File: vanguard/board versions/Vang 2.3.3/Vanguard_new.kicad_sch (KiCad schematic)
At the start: 98 parts, among them J1 USB_C_Receptacle_USB2.0_16P, J2 Micro_SD_Card_Det1, J3 Conn_02x03_Odd_Even, J4 Conn_01x03, J5 Conn_01x03, J6 Conn_01x03, J7 Conn_01x02_Pin, Q1 BSS138, Q2 BSS138, Q3 BSS138, Q4 BSS138, SW1 SW_Push, U1 TXB0104D, U11 TPS82130SILR, U12 AP2112K-3.3, U3 ATSAMD11D14A-M, U4 BMP390L, U5 BD1020HFV-TR, U6 AT25DF641A-SH-T, U7 ATmega4809-A, U8 BNO055, U9 TPS61092, Y1 Crystal

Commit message: e
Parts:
- removed D11: LED, LED_SMD:LED_0201_0603Metric, symbol Device:LED
- removed R32: 330, Resistor_SMD:R_0402_1005Metric, symbol Device:R
- removed SW1: SW_Push, symbol Switch:SW_Push
- added C10: 1uF, symbol Device:C
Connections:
- net GND: now also C10.2
- net at C16.1, R35.1, R38.1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: now also C10.1
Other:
- moved on the sheet: C18, D13, R38, U12

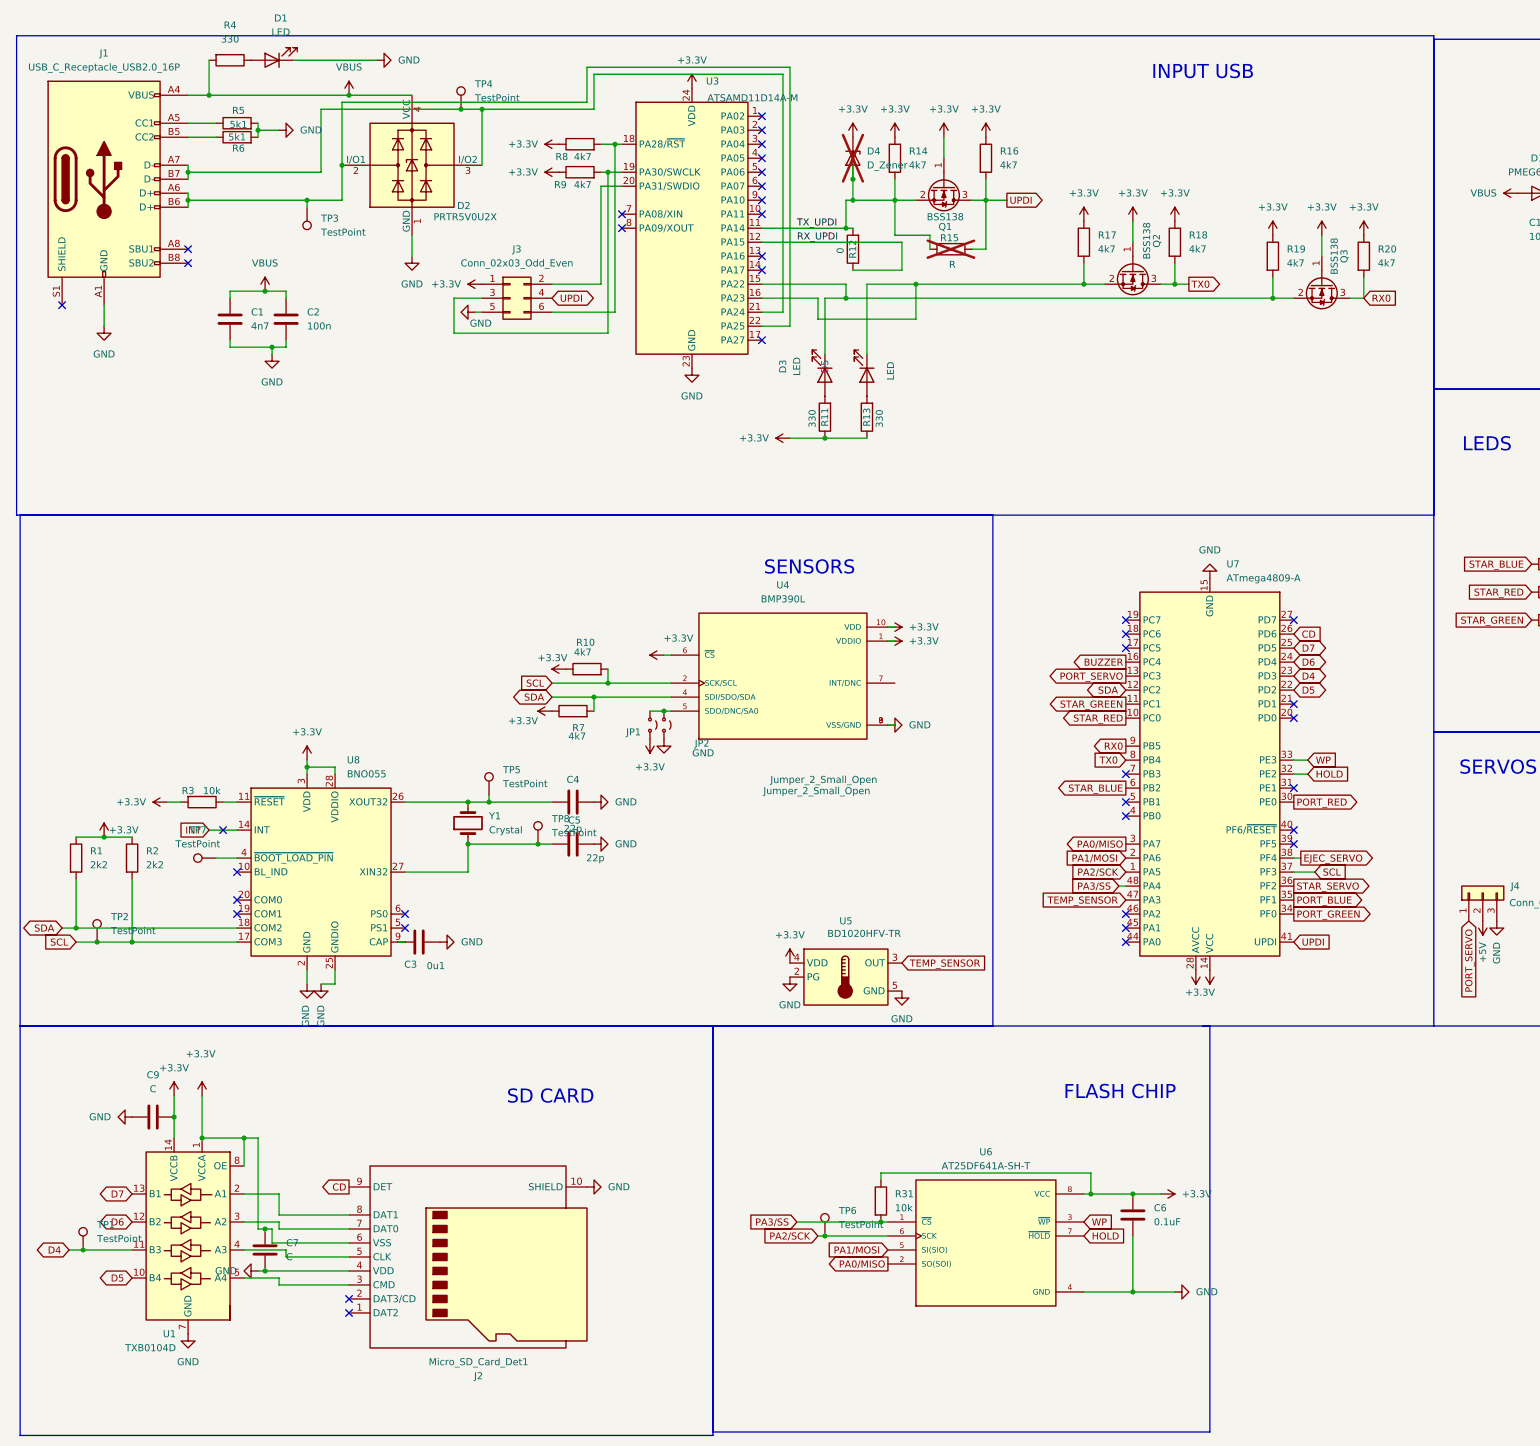
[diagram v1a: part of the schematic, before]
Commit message: updated sch caps
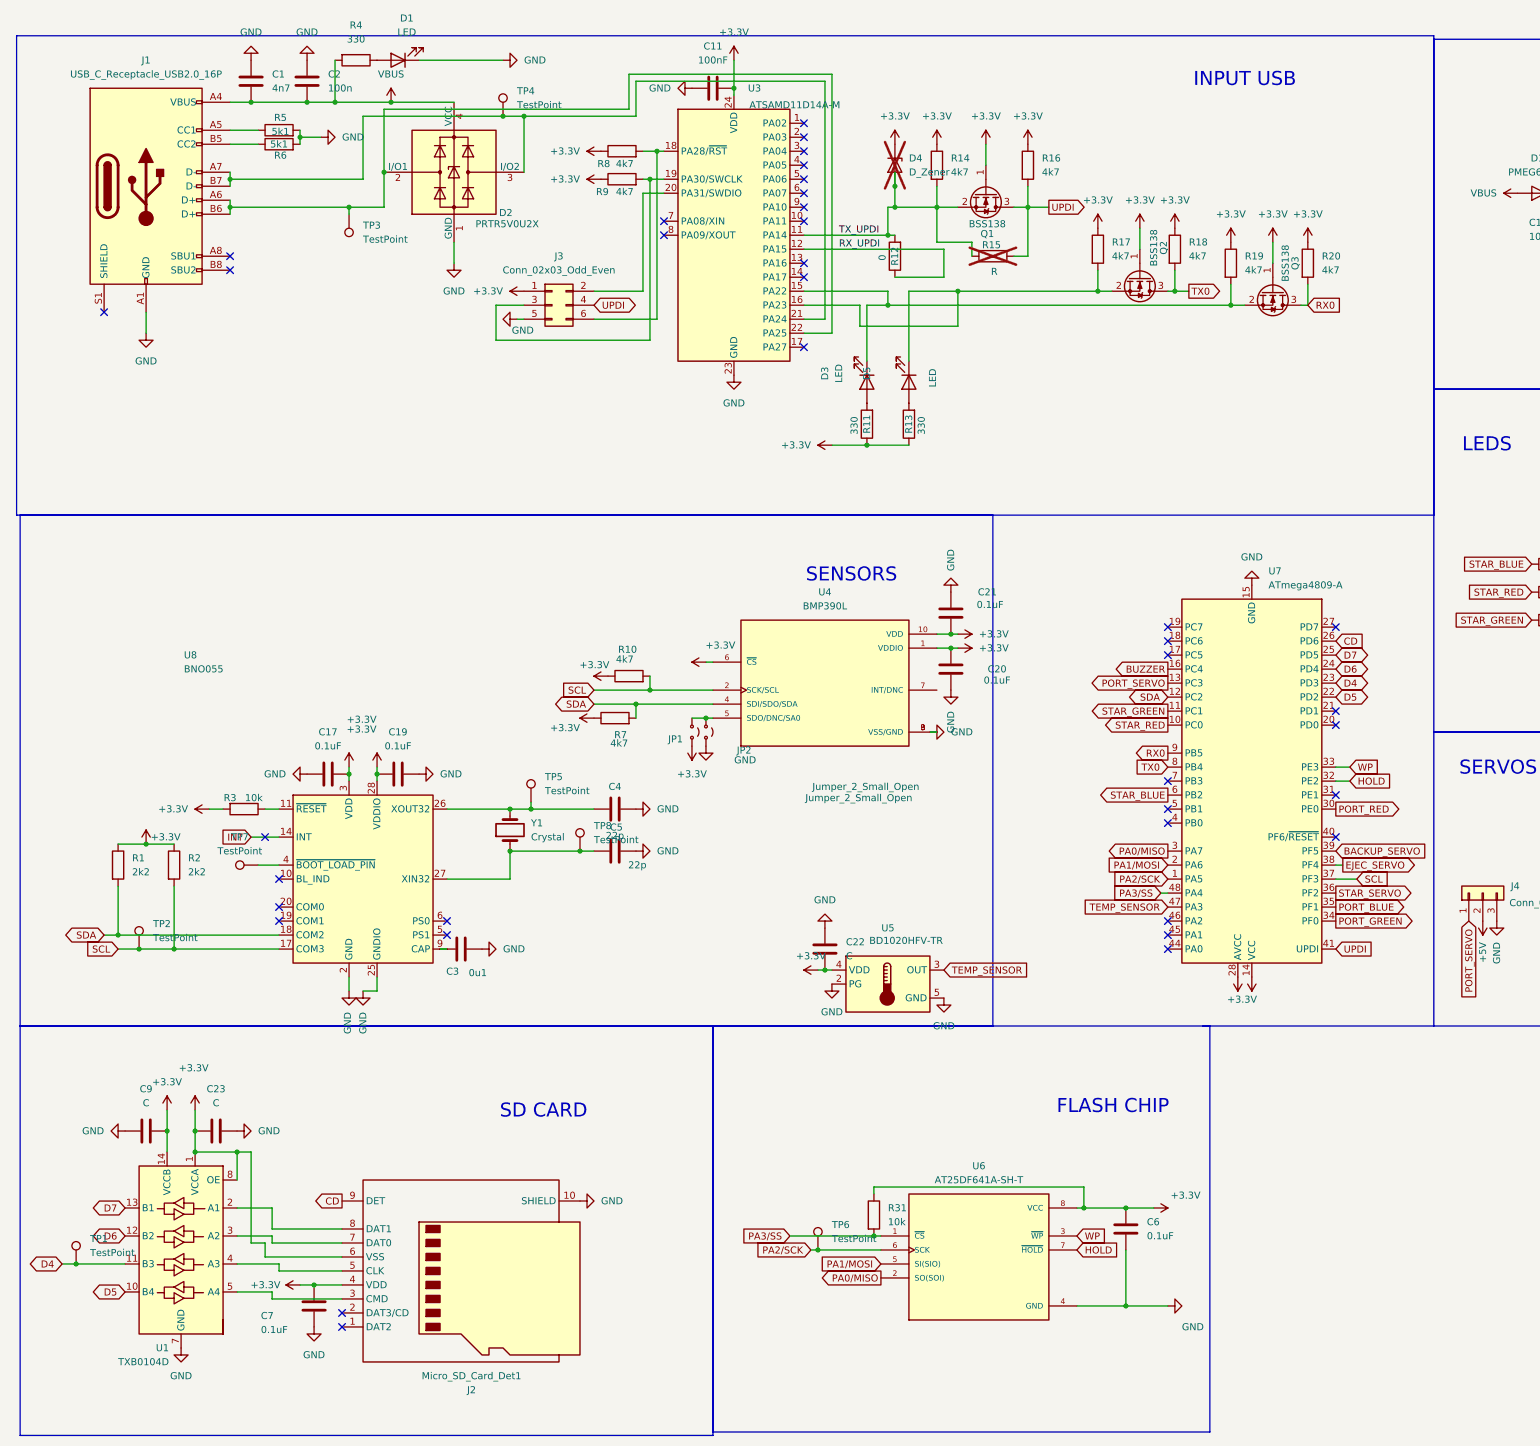
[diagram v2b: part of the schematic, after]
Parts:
- added C11: 100nF, symbol Device:C
- added C17, C19, C20, C21: 0.1uF, symbol Device:C
- added C22, C23: C, symbol Device:C
- C7: value C -> 0.1uF
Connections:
- net +3.3V: now also J2.4 (VDD), C11.2, C17.2, C19.1, C20.2, C21.1, C22.2, C23.1
- net GND: now also C1.1, C2.1, C11.1, C17.1, C19.2, C20.1, C21.2, C22.1, C23.2; no longer C1.2, C2.2, J2.4 (VDD)
- net VBUS: now also C1.2, C2.2; no longer C1.1, C2.1
- net BACKUP_SERVO: now reaches U7.39 (PF5)
- no-connect marks 39 -> 38
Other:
- moved on the sheet: C1, C2, C3, C4, C5, C6, C7, C9, D1, D2, D3, D4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
